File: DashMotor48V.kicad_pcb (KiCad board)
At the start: 4 copper layers, 71.8 x 70.7 mm, 79 parts, among them CN3(OUT)1 XT30(2+2)PB-M.G.B, CN3(OUT)2 XT30(2+2)PB-M.G.B, J1 BM07B-SRSS-TB, J2 BM07B-SRSS-TB, Q1 FDMS039N08B, Q2 FDMS039N08B, Q3 FDMS039N08B, Q4 FDMS039N08B, Q5 FDMS039N08B, Q6 FDMS039N08B, U1 TPS629203DRLR, U2 TPS629203DRLR, U3 DRV8353SRTAR, U4 STM32F446RCT6, U5 MA732GQ-Z, U6 MCP2542FD-E/MF, Y1 CSTNE8M00G550000R0

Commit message: start placing
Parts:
- U5: moved to B.Cu
- moved C15 139.1 mm to (211.5, 125.7), turned to -90 degrees
- moved C16 134.1 mm to (208.0, 125.7), turned to -90 degrees
- moved C17 129.0 mm to (204.5, 125.7), turned to -90 degrees
- moved C19 126.8 mm to (197.5, 125.7), turned to -90 degrees
- moved C18 124.0 mm to (201.0, 125.7), turned to -90 degrees
- moved C20 121.4 mm to (194.0, 125.7), turned to -90 degrees
- moved C21 116.1 mm to (190.5, 125.7), turned to -90 degrees
- moved J1 111.8 mm to (203.1, 93.2), turned to -33 degrees
- moved C22 110.9 mm to (187.0, 125.7), turned to -90 degrees
- moved VR1 106.3 mm to (209.3, 116.0)
- moved C25 106.1 mm to (176.5, 125.7), turned to -90 degrees
- moved C23 105.6 mm to (183.5, 125.7), turned to -90 degrees
- moved C26 100.6 mm to (173.0, 125.7), turned to -90 degrees
- moved C24 100.4 mm to (180.0, 125.7), turned to -90 degrees
- moved R4 95.7 mm to (201.1, 119.5)
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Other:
- outline, holes or cut-outs redrawn

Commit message: put onto the board
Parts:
- U3, U6: moved to F.Cu
- moved VR1 124.2 mm to (85.8, 103.2), turned to -90 degrees
- moved C1 119.5 mm to (86.0, 98.0)
- moved R1 113.4 mm to (81.5, 99.0), turned to -90 degrees
- moved Q1 99.5 mm to (82.0, 122.1)
- moved R4 96.6 mm to (105.7, 103.9)
- moved Q2 95.6 mm to (88.0, 122.1), turned to 180 degrees
- moved Q4 95.4 mm to (94.5, 121.0), turned to 180 degrees
- moved U2 93.5 mm to (108.7, 102.7), turned to -90 degrees
- moved H1 93.4 mm to (88.0, 129.5)
- moved C15 92.0 mm to (125.0, 94.3)
- moved C16 92.0 mm to (121.5, 94.3)
- moved C17 92.0 mm to (118.0, 94.3)
- moved C18 92.0 mm to (114.5, 94.3)
- moved C19 92.0 mm to (111.0, 94.3)
- moved C20 92.0 mm to (107.5, 94.3)
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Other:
- outline, holes or cut-outs redrawn

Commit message: have a good layout
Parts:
- C15, C16, C17, C18, C19, C20, C21, C22, C23, C24, C25, C26, C27, C28, C29, C30, C36, C4, C5, L2, L3, R4, R5, R6, U1, U2: moved to B.Cu
- moved C2 55.0 mm to (132.7, 99.6), turned to 180 degrees
- moved R2 53.0 mm to (131.9, 104.6), turned to 90 degrees
- moved C3 52.0 mm to (129.4, 97.0), turned to 180 degrees
- moved R3 49.1 mm to (129.9, 102.1), turned to 180 degrees
- moved R1 48.9 mm to (129.4, 108.6), turned to 90 degrees
- moved C1 40.6 mm to (125.0, 109.6), turned to 180 degrees
- moved VR1 39.3 mm to (125.1, 104.4), turned to 90 degrees
- moved L1 38.0 mm to (123.5, 97.6), turned to 90 degrees
- moved CN3(OUT)2 29.8 mm to (116.1, 125.2), turned to 30 degrees
- moved CN3(OUT)1 29.1 mm to (83.4, 125.4), turned to 150 degrees
- moved C11 29.0 mm to (71.6, 93.5)
- moved C29 26.6 mm to (97.9, 109.4)
- moved R4 25.0 mm to (130.1, 97.9), turned to 180 degrees
- moved C15 23.8 mm to (112.0, 114.2), turned to 90 degrees
- moved C16 23.8 mm to (108.5, 114.2), turned to 90 degrees
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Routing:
- net GND: track 0.00 -> 136.4 mm
- net +48V: track 0.00 -> 61.2 mm

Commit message: t
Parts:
- moved H3 16.3 mm to (108.2, 122.0)
- moved H1 16.1 mm to (91.8, 122.1)
- moved C6 5.82 mm to (78.2, 106.1)
- moved R12 2.53 mm to (96.3, 107.6), turned to -90 degrees
- moved R11 2.26 mm to (91.1, 107.6), turned to -90 degrees
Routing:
- net /PHASA: track 0.00 -> 17.8 mm
- net /GHA: track 0.00 -> 17.4 mm
- net /GLA: track 0.00 -> 11.5 mm
- net /SPA: track 0.00 -> 10.0 mm
- added copper zone on F.Cu, net /PHASA
- added copper zone on F.Cu, net /SPA

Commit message: 1 draft
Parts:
- moved J1 33.0 mm to (83.7, 72.1), turned to 30 degrees
- moved J2 32.7 mm to (117.3, 72.4), turned to -30 degrees
- moved C38 29.9 mm to (114.0, 87.0), turned to -90 degrees
- moved C2 18.4 mm to (114.4, 97.4), turned to 90 degrees
- moved C3 14.4 mm to (115.3, 94.2), turned to 0 degrees
- moved R2 13.9 mm to (121.7, 95.2), turned to 180 degrees
- moved C11 13.8 mm to (85.4, 92.5)
- moved R3 13.7 mm to (117.1, 97.2), turned to -90 degrees
- moved L1 13.1 mm to (111.9, 103.8), turned to 180 degrees
- moved C37 12.8 mm to (118.1, 78.5), turned to 180 degrees
- moved R1 12.4 mm to (123.6, 97.7), turned to 180 degrees
- moved C5 8.36 mm to (112.4, 93.0), turned to 180 degrees
- moved R6 8.35 mm to (112.8, 99.5), turned to 90 degrees
- moved R5 7.89 mm to (124.6, 91.4), turned to -90 degrees
- moved D1 7.27 mm to (81.4, 84.6), turned to 90 degrees
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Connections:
- net /CANH renamed /CAN+
- net /CANL renamed /CAN-
- U3 pad V: (no net) -> GND
- VR1 pad 10: (no net) -> GND
- VR1 pad 11: (no net) -> GND
- VR1 pad 12: (no net) -> GND
- VR1 pad 13: (no net) -> GND
- VR1 pad 14: (no net) -> GND
- VR1 pad 15: (no net) -> GND
- VR1 pad 16: (no net) -> GND
- VR1 pad 17: (no net) -> GND
- VR1 pad 9: unconnected-(VR1-EP-Pad9) -> GND
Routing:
- net GND: track 136.4 -> 312.8 mm, vias 0 -> 28
- net +3.3V: track 0.00 -> 148.1 mm, vias 0 -> 8
- net +48V: track 61.2 -> 152.5 mm, vias 0 -> 26
- net /CAN+: track 0.00 -> 86.1 mm, vias 0 -> 1
- net /CAN-: track 0.00 -> 85.2 mm, vias 0 -> 1
- net +12V: track 0.00 -> 68.1 mm, vias 0 -> 3
- net +5V: track 0.00 -> 46.2 mm, vias 0 -> 2
- net /TMS: track 0.00 -> 39.2 mm, vias 0 -> 2
- net /SCK: track 0.00 -> 37.0 mm, vias 0 -> 3
- net /MOSI: track 0.00 -> 36.9 mm, vias 0 -> 3
- net /MISO: track 0.00 -> 34.8 mm, vias 0 -> 3
- net /TCK: track 0.00 -> 33.9 mm, vias 0 -> 2
- net /GHC: track 0.00 -> 30.6 mm
- net /PHASC: track 0.00 -> 30.1 mm
- net /GHB: track 0.00 -> 26.8 mm
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- added copper zone on F.Cu, net +48V
- added copper zone on F.Cu, net /PHASB
- added copper zone on F.Cu, net /PHASC
- added copper zone on In1.Cu, net GND
- removed copper zone on F.Cu, net /SPA
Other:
- outline, holes or cut-outs redrawn

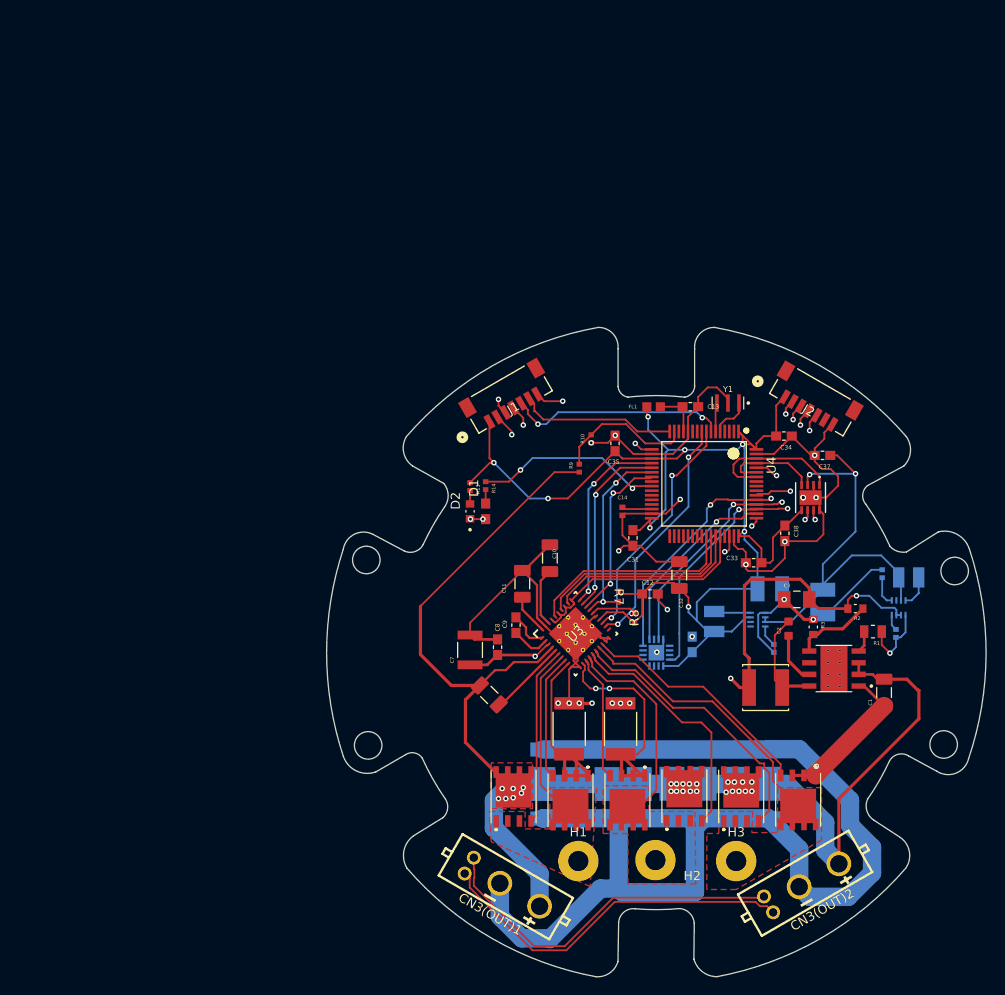
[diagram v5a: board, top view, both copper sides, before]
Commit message: power distribution + signal integrity improvements
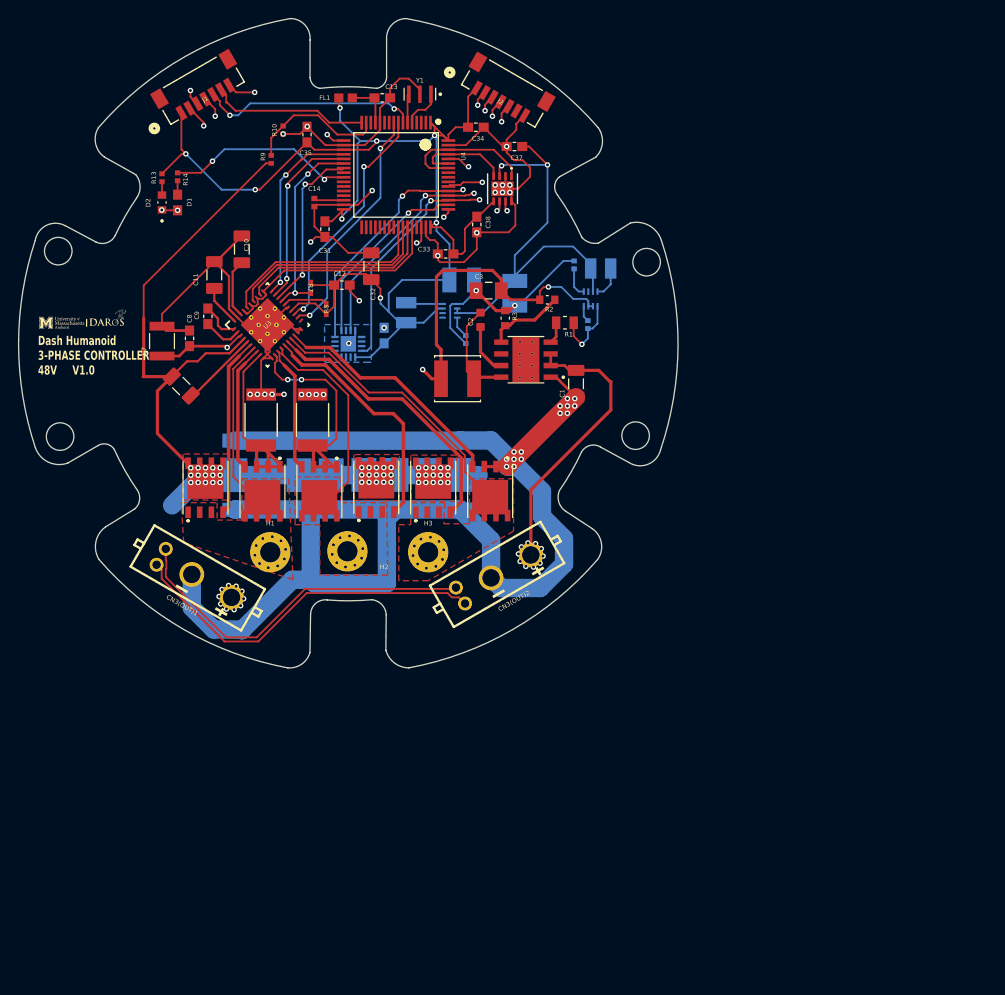
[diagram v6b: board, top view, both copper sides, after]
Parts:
- added G***: LOGO, LOGO, F.Cu at (35.2, 64.1)
- added G***: LOGO, LOGO, F.Cu at (40.2, 63.5)
- moved C1 47.5 mm to (91.2, 70.7)
- moved C10 47.5 mm to (54.8, 56.1)
- moved C11 47.5 mm to (51.8, 58.9)
- moved C13 47.5 mm to (70.1, 39.6)
- moved C15 47.5 mm to (78.6, 83.1)
- moved C16 47.5 mm to (75.1, 83.1)
- moved C17 47.5 mm to (71.6, 83.1)
- moved C18 47.5 mm to (68.1, 83.1)
- moved C19 47.5 mm to (68.1, 78.2)
- moved C2 47.5 mm to (80.8, 63.7)
- moved C20 47.5 mm to (71.6, 78.2)
- moved C21 47.5 mm to (75.1, 78.2)
- moved C30 47.5 mm to (78.6, 78.2)
- moved C31 47.5 mm to (63.9, 53.9)
- moved C32 47.5 mm to (68.9, 57.9)
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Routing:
- net +48V: track 152.5 -> 125.9 mm, vias 26 -> 65
- net GND: track 312.8 -> 314.3 mm, vias 28 -> 46
- net /PHASC: track 30.1 -> 29.9 mm, vias 0 -> 10
- net /PHASB: track 23.1 -> 23.0 mm, vias 0 -> 10
- net /PHASA: vias 0 -> 10
- added copper zone on In2.Cu, net +48V
- added copper zone on B.Cu, net GND
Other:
- board text added: "Dash Humanoid 3-PHASE CONTROLLER 48V V1.0"

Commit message: will start 2nd version
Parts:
- moved C1 90.1 mm to (174.8, 104.4)
- moved C2 90.1 mm to (164.4, 97.4)
- moved C26 90.1 mm to (137.6, 111.9)
- moved C27 90.1 mm to (141.1, 111.9)
- moved C28 90.1 mm to (144.6, 111.9)
- moved C29 90.1 mm to (148.1, 111.9)
- moved C36 90.1 mm to (153.9, 99.1)
- moved H2 90.1 mm to (149.9, 122.6)
- moved C10 90.1 mm to (138.4, 89.7)
- moved C11 90.1 mm to (135.4, 92.5)
- moved C19 90.1 mm to (151.7, 111.9)
- moved C20 90.1 mm to (155.2, 111.9)
- moved C21 90.1 mm to (158.7, 111.9)
- moved C22 90.1 mm to (148.1, 116.7)
- moved C23 90.1 mm to (144.6, 116.7)
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
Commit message: Add files via upload
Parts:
- H1, H2, H3: value MountingHole_Pad -> Phase A; footprint MountingHole:MountingHole_2.2mm_M2_Pad -> dash:Pad_Square_Vias_6.5x6.5mm
- moved G*** 48.8 mm to (162.8, 126.5)
- moved G*** 48.8 mm to (157.8, 127.0)
- moved CN3(OUT)1 28.3 mm to (121.5, 99.7), turned to 90 degrees
- moved CN3(OUT)2 28.1 mm to (178.0, 99.7), turned to 90 degrees
- moved L2 7.84 mm to (171.3, 87.0)
- moved C1 6.69 mm to (171.6, 110.2)
- moved U2 5.19 mm to (173.4, 90.9)
- moved R5 4.64 mm to (170.4, 89.5), turned to 0 degrees
- moved C7 4.43 mm to (130.0, 95.3)
- moved R4 4.41 mm to (172.4, 95.5)
- moved C11 3.91 mm to (132.5, 89.9)
- moved C10 3.86 mm to (136.1, 86.6)
- moved C6 3.62 mm to (129.2, 107.1), turned to 90 degrees
- moved H1 2.13 mm to (139.5, 122.1), turned to 90 degrees
- moved R11 1.67 mm to (141.0, 106.7)
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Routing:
- net +48V: track 125.9 -> 38.8 mm, vias 65 -> 82
- net GND: track 314.3 -> 247.8 mm, vias 46 -> 72
- net /SPA: track 22.9 -> 10.4 mm
- net /CAN+: track 86.1 -> 74.2 mm, vias 1 -> 3
- net /SPB: track 26.2 -> 14.6 mm
- net /CAN-: track 85.2 -> 74.3 mm, vias 1 -> 3
- net +5V: track 46.2 -> 38.5 mm, vias 2 -> 4
- net Net-(U3-VCP): track 8.55 -> 13.5 mm
- net Net-(U3-VGLS): track 4.41 -> 8.74 mm
- net +3.3V: track 148.1 -> 151.8 mm
- net Net-(U3-DVDD): track 6.38 -> 9.63 mm
- net Net-(VR1-FB): track 8.56 -> 6.60 mm
- net /GLA: track 13.7 -> 11.8 mm
- net Net-(U2-MODE/S-CONF): track 1.75 -> 3.53 mm
- net /GHC: track 30.5 -> 28.8 mm
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- added copper zone on F.Cu, net /SPA
- added copper zone on F.Cu, net /SPB
- added copper zone on F.Cu, net GND
- added copper zone on In4.Cu, net GND
- removed copper zone on B.Cu, net GND
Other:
- copper layers 4 -> 6
